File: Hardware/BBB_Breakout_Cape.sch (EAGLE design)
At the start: 27 parts, among them U1 EEPROM-I2CSMD

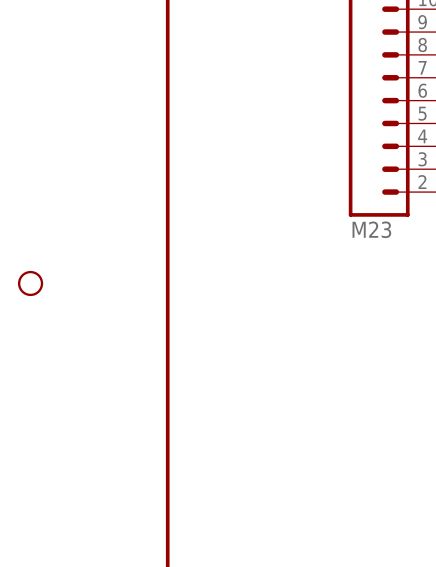
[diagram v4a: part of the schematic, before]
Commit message: added more labels and fixed drill hole
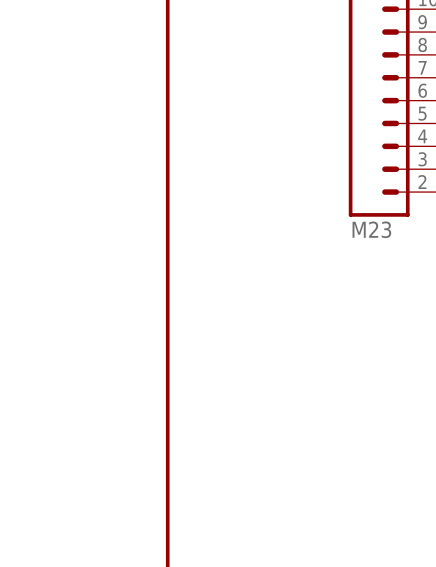
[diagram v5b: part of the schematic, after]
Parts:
- removed STANDOFF1: STAND-OFF, SparkFun-Electromechanical:STAND-OFF
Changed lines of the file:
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@@
 <part name="JP1" library="SparkFun-Connectors" deviceset="M01" device="PTH"/>
 <part name="JP2" library="SparkFun-Connectors" deviceset="M01" device="PTH"/>
-<part name="STANDOFF1" library="SparkFun-Electromechanical" deviceset="STAND-OFF" device=""/>
 </parts>
 <sheets>
@@
 <instance part="JP1" gate="G$1" x="177.8" y="83.82"/>
 <instance part="JP2" gate="G$1" x="177.8" y="71.12"/>
-<instance part="STANDOFF1" gate="G$1" x="-15.24" y="91.44"/>
 </instances>
 <busses>

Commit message: added version number
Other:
- note added: "v10"
- note removed: "v01"
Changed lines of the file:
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@@
 <text x="137.16" y="3.81" size="1.778" layer="97" align="bottom-center">0x57</text>
 <text x="176.53" y="11.43" size="2.54" layer="94" align="bottom-center">Casey Kuhns</text>
-<text x="241.3" y="7.62" size="2.54" layer="94" align="bottom-center">v01</text>
+<text x="241.3" y="7.62" size="2.54" layer="94" align="bottom-center">v10</text>
 <text x="102.87" y="67.31" size="1.27" layer="97" align="bottom-center">WP default is off
 Pull high to enable</text>

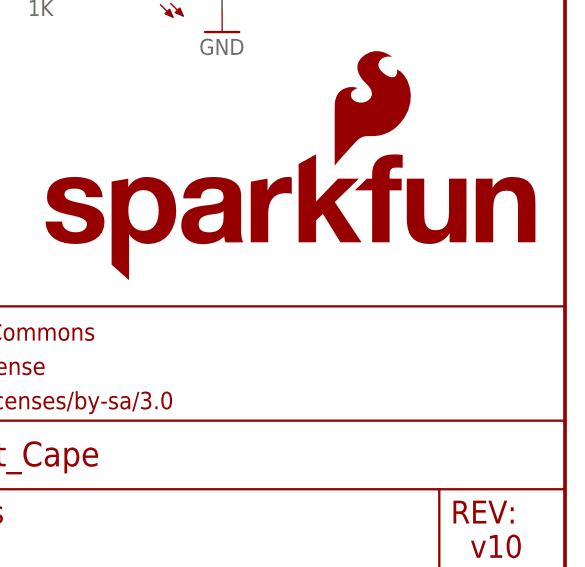
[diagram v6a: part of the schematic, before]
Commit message: added local fiducials
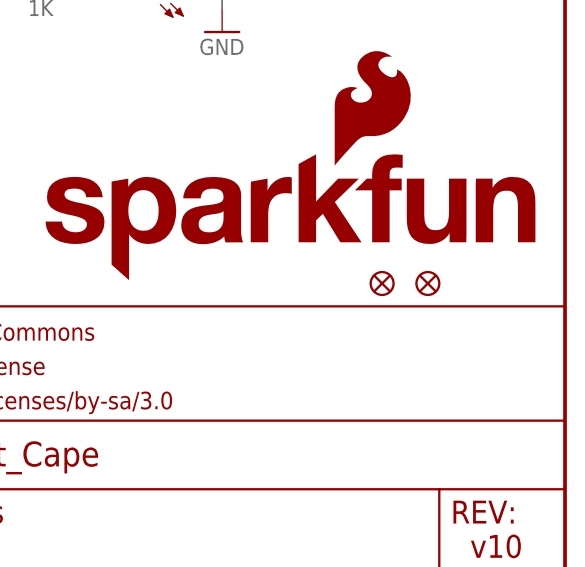
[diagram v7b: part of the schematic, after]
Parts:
- added FID1, FID2: FIDUCIAL1X2, SparkFun-Aesthetics:FIDUCIAL1X2
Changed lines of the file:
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@@
 <part name="JP1" library="SparkFun-Connectors" deviceset="M01" device="PTH"/>
 <part name="JP2" library="SparkFun-Connectors" deviceset="M01" device="PTH"/>
+<part name="FID1" library="SparkFun-Aesthetics" deviceset="FIDUCIAL" device="1X2"/>
+<part name="FID2" library="SparkFun-Aesthetics" deviceset="FIDUCIAL" device="1X2"/>
 </parts>
 <sheets>
@@
 <instance part="JP1" gate="G$1" x="177.8" y="83.82"/>
 <instance part="JP2" gate="G$1" x="177.8" y="71.12"/>
+<instance part="FID1" gate="G$1" x="228.6" y="38.1"/>
+<instance part="FID2" gate="G$1" x="233.68" y="38.1"/>
 </instances>
 <busses>

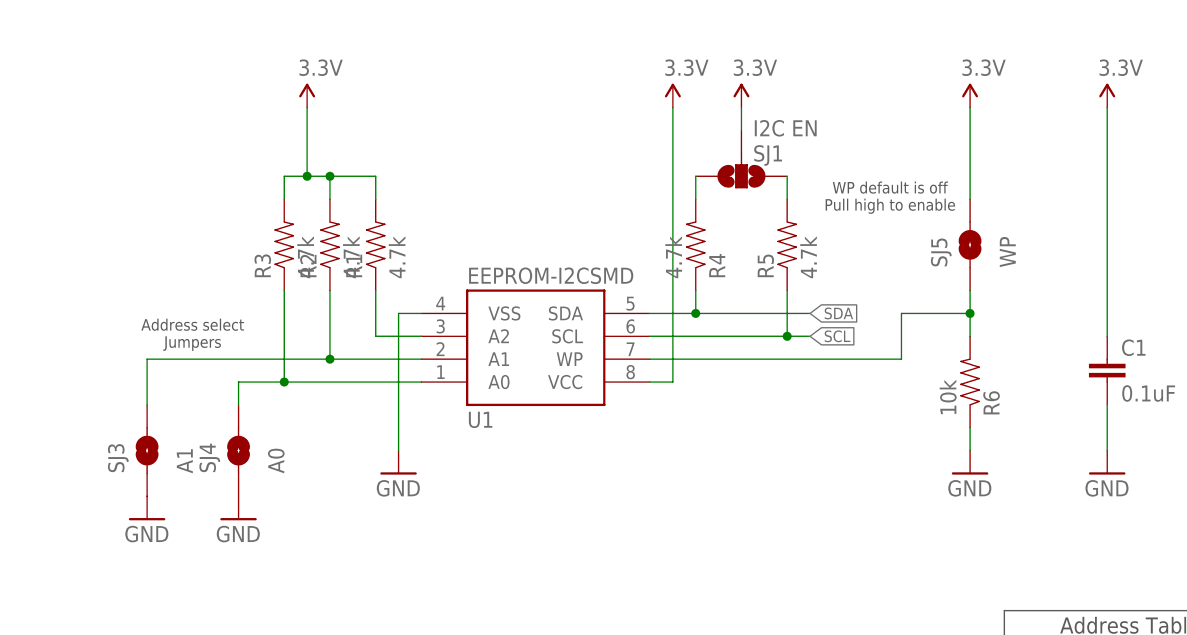
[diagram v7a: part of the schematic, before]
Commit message: Updated juper packages on design and panel.  This only effects tcream layer.
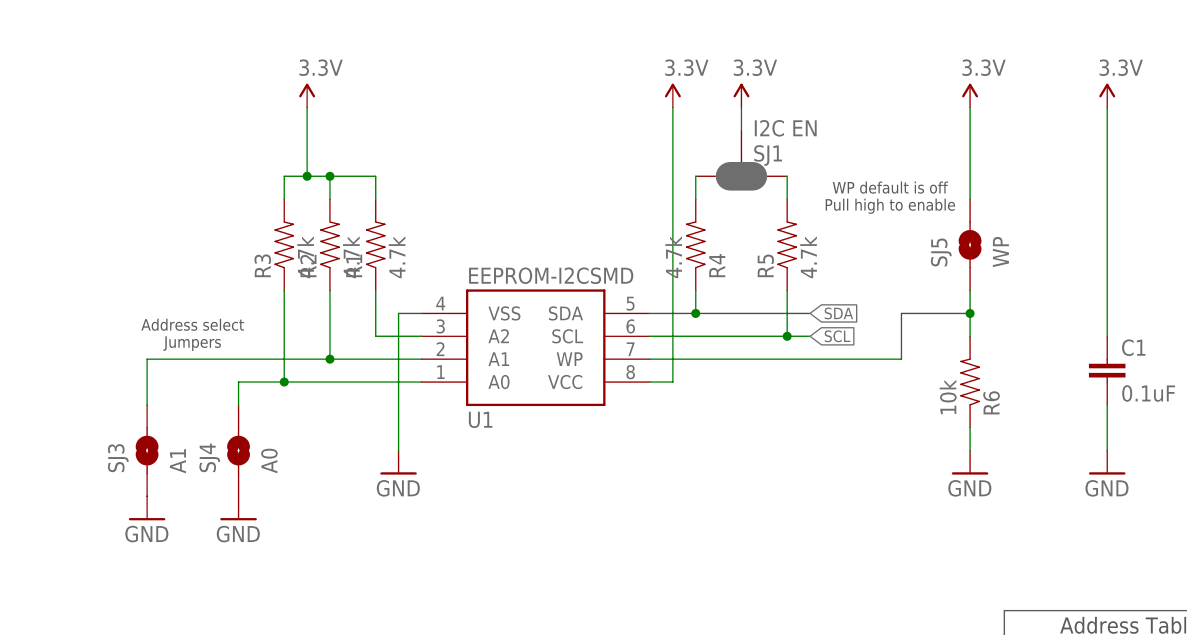
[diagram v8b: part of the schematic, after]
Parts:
- SJ1: device SparkFun-Passives:SOLDERJUMPER_2WAYPASTE1&2&3 -> SparkFun-Jumpers:JUMPER-SMT_3_2-NC_PASTE_SILK
- SJ3, SJ4, SJ5: device SparkFun-Passives:SOLDERJUMPERNO -> SparkFun-Jumpers:JUMPER-SMT_2_NO_SILK
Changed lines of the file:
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@@
 <?xml version="1.0" encoding="utf-8"?>
 <!DOCTYPE eagle SYSTEM "eagle.dtd">
-<eagle version="6.5.0">
+<eagle version="7.7.0">
 <drawing>
 <settings>
@@
 <layer number="54" name="bGND_GNDA" color="1" fill="9" visible="no" active="no"/>
 <layer number="56" name="wert" color="7" fill="1" visible="no" active="no"/>
+<layer number="57" name="tCAD" color="7" fill="1" visible="no" active="no"/>
+<layer number="59" name="tCarbon" color="7" fill="1" visible="no" active="no"/>
+<layer number="60" name="bCarbon" color="7" fill="1" visible="no" active="no"/>
+<layer number="90" name="Modules" color="5" fill="1" visible="yes" active="yes"/>
 <layer number="91" name="Nets" color="2" fill="1" visible="yes" active="yes"/>
 <layer number="92" name="Busses" color="1" fill="1" visible="yes" active="yes"/>
@@
 <layer number="97" name="Info" color="7" fill="1" visible="yes" active="yes"/>
 <layer number="98" name="Guide" color="6" fill="1" visible="yes" active="yes"/>
+<layer number="99" name="SpiceOrder" color="7" fill="1" visible="no" active="no"/>
 <layer number="100" name="Muster" color="7" fill="1" visible="no" active="no"/>
 <layer number="101" name="Patch_Top" color="12" fill="4" visible="yes" active="yes"/>
@@
 <layer number="108" name="tplace-old" color="10" fill="1" visible="yes" active="yes"/>
 <layer number="109" name="ref-old" color="11" fill="1" visible="yes" active="yes"/>
+<layer number="110" name="fp0" color="7" fill="1" visible="yes" active="yes"/>
+<layer number="111" name="LPC17xx" color="7" fill="1" visible="yes" active="yes"/>
+<layer number="112" name="tSilk" color="7" fill="1" visible="yes" active="yes"/>
+<layer number="113" name="IDFDebug" color="7" fill="1" visible="yes" active="yes"/>
 <layer number="116" name="Patch_BOT" color="9" fill="4" visible="yes" active="yes"/>
+<layer number="118" name="Rect_Pads" color="7" fill="1" visible="yes" active="yes"/>
 <layer number="121" name="_tsilk" color="7" fill="1" visible="yes" active="yes"/>
 <layer number="122" name="_bsilk" color="7" fill="1" visible="yes" active="yes"/>
+<layer number="123" name="tTestmark" color="7" fill="1" visible="yes" active="yes"/>
+<layer number="124" name="bTestmark" color="7" fill="1" visible="yes" active="yes"/>
 <layer number="125" name="_tNames" color="7" fill="1" visible="yes" active="yes"/>
+<layer number="126" name="_bNames" color="7" fill="1" visible="yes" active="yes"/>
+<layer number="127" name="_tValues" color="7" fill="1" visible="yes" active="yes"/>
+<layer number="128" name="_bValues" color="7" fill="1" visible="yes" active="yes"/>
+<layer number="129" name="Mask" color="7" fill="1" visible="yes" active="yes"/>
+<layer number="131" name="tAdjust" color="7" fill="1" visible="yes" active="yes"/>
+<layer number="132" name="bAdjust" color="7" fill="1" visible="yes" active="yes"/>
 <layer number="144" name="Drill_legend" color="7" fill="1" visible="yes" active="yes"/>
+<layer number="150" name="Notes" color="7" fill="1" visible="yes" active="yes"/>
 <layer number="151" name="HeatSink" color="7" fill="1" visible="yes" active="yes"/>
+<layer number="152" name="_bDocu" color="7" fill="1" visible="yes" active="yes"/>
+<layer number="153" name="FabDoc1" color="7" fill="1" visible="yes" active="yes"/>
+<layer number="154" name="FabDoc2" color="7" fill="1" visible="yes" active="yes"/>
+<layer number="155" name="FabDoc3" color="7" fill="1" visible="yes" active="yes"/>
 <layer number="199" name="Contour" color="7" fill="1" visible="yes" active="yes"/>
 <layer number="200" name="200bmp" color="1" fill="10" visible="yes" active="yes"/>
@@
 <layer number="223" name="223bmp" color="24" fill="1" visible="no" active="no"/>
 <layer number="224" name="224bmp" color="25" fill="1" visible="no" active="no"/>
+<layer number="225" name="225bmp" color="7" fill="1" visible="yes" active="yes"/>
+<layer number="226" name="226bmp" color="7" fill="1" visible="yes" active="yes"/>
+<layer number="227" name="227bmp" color="7" fill="1" visible="yes" active="yes"/>
+<layer number="228" name="228bmp" color="7" fill="1" visible="yes" active="yes"/>
+<layer number="229" name="229bmp" color="7" fill="1" visible="yes" active="yes"/>
+<layer number="230" name="230bmp" color="7" fill="1" visible="yes" active="yes"/>
+<layer number="231" name="231bmp" color="7" fill="1" visible="yes" active="yes"/>
+<layer number="248" name="Housing" color="7" fill="1" visible="yes" active="yes"/>
+<layer number="249" name="Edge" color="7" fill="1" visible="yes" active="yes"/>
 <layer number="250" name="Descript" color="3" fill="1" visible="no" active="no"/>
 <layer number="251" name="SMDround" color="12" fill="11" visible="no" active="no"/>
 <layer number="254" name="cooling" color="7" fill="1" visible="yes" active="yes"/>
+<layer number="255" name="routoute" color="7" fill="1" visible="yes" active="yes"/>
 </layers>
 <schematic xreflabel="%F%N/%S.%C%R" xrefpart="/%S.%C%R">
@@
 <attribute name="PROD_ID" value="RES-07857"/>
 </part>
-<part name="SJ1" library="SparkFun-Passives" deviceset="SOLDERJUMPER_2WAY" device="PASTE1&amp;2&amp;3" value="I2C EN"/>
+<part name="SJ1" library="SparkFun-Jumpers" deviceset="JUMPER-SMT_3_2-NC_PASTE" device="_SILK" value="I2C EN"/>
 <part name="R6" library="SparkFun-Resistors" deviceset="10KOHM1/10W1%(0603)" device="0603" value="10k"/>
 <part name="SUPPLY4" library="SparkFun-Aesthetics" deviceset="3.3V" device=""/>
@@
 <part name="SUPPLY8" library="SparkFun-Aesthetics" deviceset="5V" device=""/>
 <part name="SUPPLY9" library="SparkFun-Aesthetics" deviceset="5V" device=""/>
-<part name="SJ3" library="SparkFun-Passives" deviceset="SOLDERJUMPER" device="NO" value="A1"/>
-<part name="SJ4" library="SparkFun-Passives" deviceset="SOLDERJUMPER" device="NO" value="A0"/>
+<part name="SJ3" library="SparkFun-Jumpers" deviceset="JUMPER-SMT_2_NO" device="_SILK" value="A1"/>
+<part name="SJ4" library="SparkFun-Jumpers" deviceset="JUMPER-SMT_2_NO" device="_SILK" value="A0"/>
 <part name="GND2" library="SparkFun-Aesthetics" deviceset="GND" device=""/>
 <part name="GND9" library="SparkFun-Aesthetics" deviceset="GND" device=""/>
-<part name="SJ5" library="SparkFun-Passives" deviceset="SOLDERJUMPER" device="NO" value="WP"/>
+<part name="SJ5" library="SparkFun-Jumpers" deviceset="JUMPER-SMT_2_NO" device="_SILK" value="WP"/>
 <part name="D1" library="SparkFun-LED" deviceset="LED-RED" device="0603" value="RED"/>
 <part name="D2" library="SparkFun-LED" deviceset="LED-RED" device="0603" value="RED"/>
@@
 <instance part="SUPPLY8" gate="G$1" x="33.02" y="165.1"/>
 <instance part="SUPPLY9" gate="G$1" x="101.6" y="167.64"/>
-<instance part="SJ3" gate="1" x="20.32" y="40.64" rot="R90"/>
-<instance part="SJ4" gate="1" x="30.48" y="40.64" rot="R90"/>
+<instance part="SJ3" gate="G$1" x="20.32" y="40.64" rot="R90"/>
+<instance part="SJ4" gate="G$1" x="30.48" y="40.64" rot="R90"/>
 <instance part="GND2" gate="1" x="30.48" y="33.02"/>
 <instance part="GND9" gate="1" x="20.32" y="33.02"/>
-<instance part="SJ5" gate="1" x="111.76" y="63.5" rot="R90"/>
+<instance part="SJ5" gate="G$1" x="111.76" y="63.5" rot="R90"/>
 <instance part="D1" gate="G$1" x="203.2" y="83.82" rot="R90"/>
 <instance part="D2" gate="G$1" x="203.2" y="71.12" rot="R90"/>
@@
 <pinref part="SUPPLY5" gate="G$1" pin="3.3V"/>
 <wire x1="111.76" y1="78.74" x2="111.76" y2="68.58" width="0.1524" layer="91"/>
-<pinref part="SJ5" gate="1" pin="2"/>
+<pinref part="SJ5" gate="G$1" pin="2"/>
 </segment>
 <segment>
@@
 </segment>
 <segment>
-<pinref part="SJ4" gate="1" pin="1"/>
+<pinref part="SJ4" gate="G$1" pin="1"/>
 <pinref part="GND2" gate="1" pin="GND"/>
 </segment>
 <segment>
-<pinref part="SJ3" gate="1" pin="1"/>
+<pinref part="SJ3" gate="G$1" pin="1"/>
 <pinref part="GND9" gate="1" pin="GND"/>
 </segment>
@@
 <wire x1="40.64" y1="50.8" x2="20.32" y2="50.8" width="0.1524" layer="91"/>
 <junction x="40.64" y="50.8"/>
-<pinref part="SJ3" gate="1" pin="2"/>
+<pinref part="SJ3" gate="G$1" pin="2"/>
 <wire x1="20.32" y1="50.8" x2="20.32" y2="45.72" width="0.1524" layer="91"/>
 </segment>
@@
 <wire x1="35.56" y1="48.26" x2="35.56" y2="58.42" width="0.1524" layer="91"/>
 <junction x="35.56" y="48.26"/>
-<pinref part="SJ4" gate="1" pin="2"/>
+<pinref part="SJ4" gate="G$1" pin="2"/>
 <wire x1="35.56" y1="48.26" x2="30.48" y2="48.26" width="0.1524" layer="91"/>
 <wire x1="30.48" y1="48.26" x2="30.48" y2="45.72" width="0.1524" layer="91"/>
@@
 <net name="N$1" class="0">
 <segment>
-<pinref part="SJ5" gate="1" pin="1"/>
+<pinref part="SJ5" gate="G$1" pin="1"/>
 <pinref part="R6" gate="G$1" pin="2"/>
 <wire x1="111.76" y1="58.42" x2="111.76" y2="55.88" width="0.1524" layer="91"/>
